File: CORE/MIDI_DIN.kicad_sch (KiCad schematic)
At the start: 62 parts, among them J1 Conn_02x08_Odd_Even, J2 USB_C_Receptacle_USB2.0, J3 Conn_01x04, J5 MAB5100S, J6 MAB5100S, J7 Conn_01x06, Q1 BSS84, Q2 2N7002, Q5 2N7002, SW1 SW_Slide_SPDT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

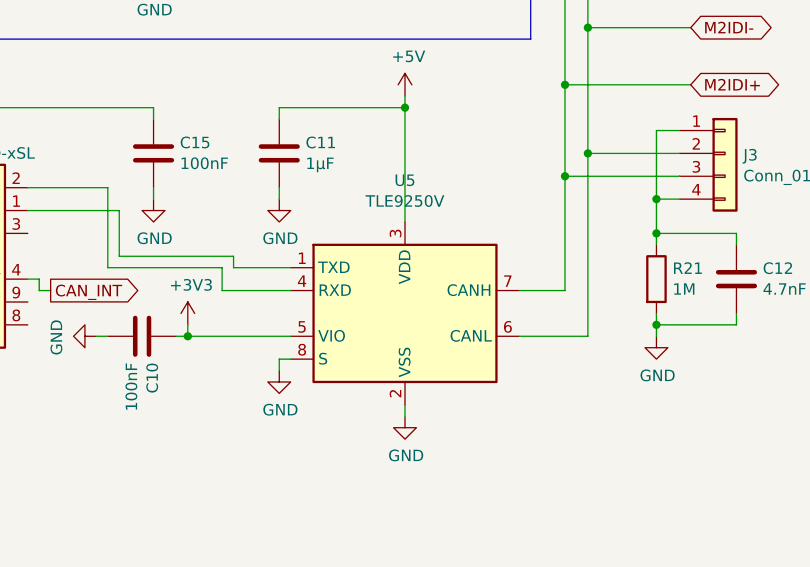
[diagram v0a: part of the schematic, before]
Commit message: Change CAN tranceiver to MCP2562
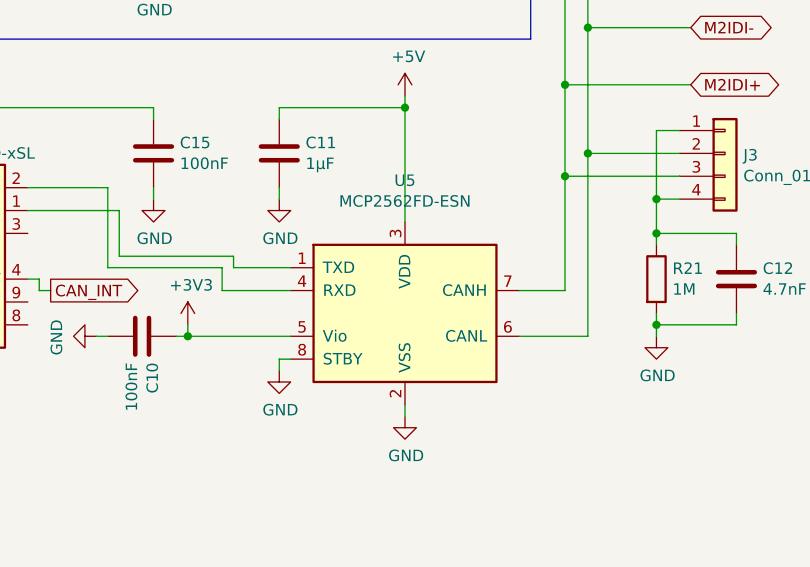
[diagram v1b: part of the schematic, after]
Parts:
- U5: value TLE9250V -> MCP2562FD-ESN; footprint Package_SO:Infineon_PG-DSO-8-27_3.9x4.9mm_EP2.65x3mm -> Package_SO:SOIC-8_3.9x4.9mm_P1.27mm; symbol Interface_CAN_LIN:MCP2558FD-xMF -> Interface_CAN_LIN:MCP2562-E-SN
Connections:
- net GND: no longer U5.9 (VSS)
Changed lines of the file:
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@@
     )
   )
-  (symbol (lib_id "Interface_CAN_LIN:MCP2558FD-xMF") (at 232.41 148.59 0) (unit 1)
+  (symbol (lib_id "Interface_CAN_LIN:MCP2562-E-SN") (at 232.41 148.59 0) (unit 1)
     (in_bom yes) (on_board yes) (dnp no)
     (property "Reference" "U5" (at 232.41 133.8326 0)
       (effects (font (size 1.27 1.27)))
     )
-    (property "Value" "TLE9250V" (at 232.41 136.144 0)
+    (property "Value" "MCP2562FD-ESN" (at 232.41 136.144 0)
       (effects (font (size 1.27 1.27)))
     )
-    (property "Footprint" "Package_SO:Infineon_PG-DSO-8-27_3.9x4.9mm_EP2.65x3mm" (at 232.41 163.83 0)
-      (effects (font (size 1.27 1.27)) hide)
+    (property "Footprint" "Package_SO:SOIC-8_3.9x4.9mm_P1.27mm" (at 232.41 161.29 0)
+      (effects (font (size 1.27 1.27) italic) hide)
     )
-    (property "Datasheet" "https://ww1.microchip.com/downloads/en/DeviceDoc/20005533A.pdf" (at 232.41 148.59 0)
+    (property "Datasheet" "http://ww1.microchip.com/downloads/en/DeviceDoc/25167A.pdf" (at 232.41 148.59 0)
       (effects (font (size 1.27 1.27)) hide)
     )
@@
     (pin "7")
     (pin "8")
-    (pin "9")
     (instances
       (project "MIDI_DIN"

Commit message: Finalize module
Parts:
- C13, C14: value 15pF -> 12pF
- J5, J6: footprint Custom_FP:DIN-5_Hirschmann_MAB5100S -> Custom_FP:DIN-5_Hirschmann
- R18, R19: footprint Resistor_SMD:R_0603_1608Metric -> Resistor_SMD:R_0805_2012Metric
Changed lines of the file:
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@@
       (effects (font (size 1.27 1.27)) (justify right))
     )
-    (property "Footprint" "Custom_FP:DIN-5_Hirschmann_MAB5100S" (at 267.97 43.18 0)
+    (property "Footprint" "Custom_FP:DIN-5_Hirschmann" (at 267.97 43.18 0)
       (effects (font (size 1.27 1.27)) hide)
     )
@@
       (effects (font (size 1.27 1.27)) (justify right))
     )
-    (property "Footprint" "Custom_FP:DIN-5_Hirschmann_MAB5100S" (at 219.71 74.93 0)
+    (property "Footprint" "Custom_FP:DIN-5_Hirschmann" (at 219.71 74.93 0)
       (effects (font (size 1.27 1.27)) hide)
     )
@@
       (effects (font (size 1.27 1.27)) (justify left))
     )
-    (property "Footprint" "Resistor_SMD:R_0603_1608Metric" (at 270.51 80.772 90)
+    (property "Footprint" "Resistor_SMD:R_0805_2012Metric" (at 270.51 80.772 90)
       (effects (font (size 1.27 1.27)) hide)
     )
@@
       (effects (font (size 1.27 1.27)) (justify left))
     )
-    (property "Footprint" "Resistor_SMD:R_0603_1608Metric" (at 270.51 90.932 90)
+    (property "Footprint" "Resistor_SMD:R_0805_2012Metric" (at 270.51 90.932 90)
       (effects (font (size 1.27 1.27)) hide)
     )
@@
       (effects (font (size 1.27 1.27)) (justify left))
     )
-    (property "Value" "15pF" (at 142.24 140.97 90)
+    (property "Value" "12pF" (at 142.24 140.97 90)
       (effects (font (size 1.27 1.27)) (justify left))
     )
@@
       (effects (font (size 1.27 1.27)) (justify left))
     )
-    (property "Value" "15pF" (at 142.24 158.75 90)
-      (effects (font (size 1.27 1.27)) (justify left))
-    )
+    (property "Value" "12pF" (at 142.24 158.75 90)
+      (effects (font (size 1.27 1.27)) (justify left))
+    )

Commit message: Add warning about bootloader
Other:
- note added: "WARNING! Could not get the bootloader running on this MCU. consider using ATSAMD21G17 if you want to use the SAM-BA bootloader. It should be pin compatible"
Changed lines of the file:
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@@
     (stroke (width 0) (type default))
+  )
+  (text "WARNING!\nCould not get the bootloader running on this MCU.\nconsider using ATSAMD21G17 if you want to use the \nSAM-BA bootloader. It should be pin compatible"
+    (at 76.2 145.415 0)
+    (effects (font (size 1.27 1.27)) (justify left bottom))
   )
   (global_label "SPI_MISO" (shape input) (at 114.3 57.15 0)
